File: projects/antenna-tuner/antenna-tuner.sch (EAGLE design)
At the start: 32 parts, among them J1 Power Jack, J2 RJ45, J3 RJ45, M1 SERVO, Q1 IRF5305, Q2 BC337, U1 Arduino Pro Mini

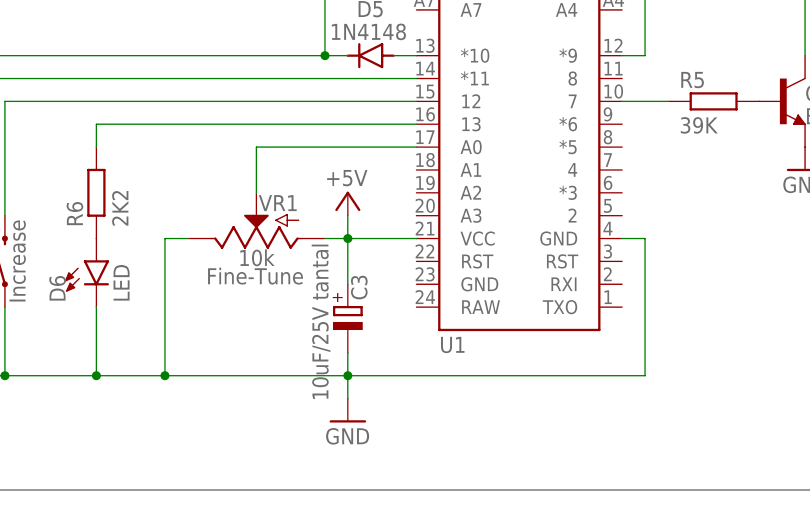
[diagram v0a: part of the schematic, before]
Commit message: Updated antenna tuner schematic
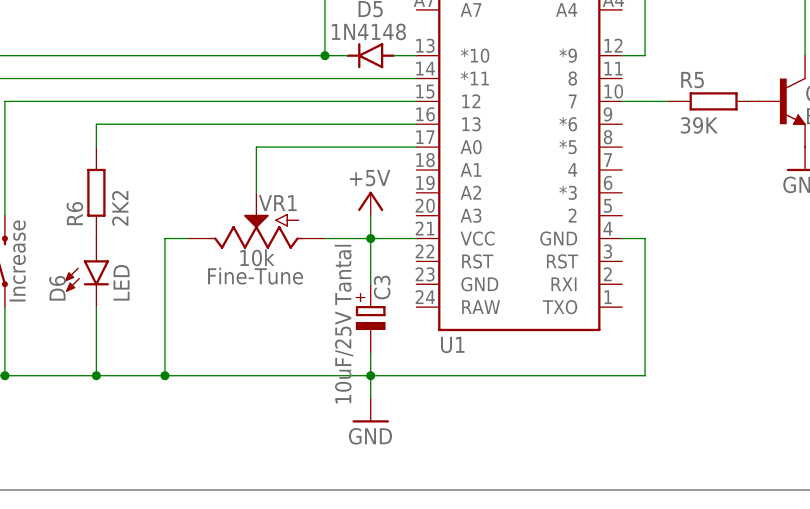
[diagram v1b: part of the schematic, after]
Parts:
- C3: value 10uF/25V tantal -> 10uF/25V Tantal
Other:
- moved on the sheet: C3
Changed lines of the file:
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@@
 <part name="J3" library="SparkFun-Connectors" library_urn="urn:adsk.eagle:library:513" deviceset="RJ45-8" device="" package3d_urn="urn:adsk.eagle:package:38235/1" value="RJ45"/>
 <part name="C1" library="rcl" library_urn="urn:adsk.eagle:library:334" deviceset="CPOL-EU" device="E5-10.5" package3d_urn="urn:adsk.eagle:package:23372/1" value="1000uF/25V"/>
-<part name="C3" library="rcl" library_urn="urn:adsk.eagle:library:334" deviceset="CPOL-EU" device="E2.5-6" package3d_urn="urn:adsk.eagle:package:23349/1" value="10uF/25V tantal"/>
+<part name="C3" library="rcl" library_urn="urn:adsk.eagle:library:334" deviceset="CPOL-EU" device="E2.5-6" package3d_urn="urn:adsk.eagle:package:23349/1" value="10uF/25V Tantal"/>
 <part name="R2" library="rcl" library_urn="urn:adsk.eagle:library:334" deviceset="R-EU_" device="0207/7" package3d_urn="urn:adsk.eagle:package:23493/2" value="196"/>
 <part name="R3" library="rcl" library_urn="urn:adsk.eagle:library:334" deviceset="R-EU_" device="0207/7" package3d_urn="urn:adsk.eagle:package:23493/2" value="196"/>
@@
 <attribute name="VALUE" x="-86.233" y="55.3466" size="1.778" layer="96"/>
 </instance>
-<instance part="C3" gate="G$1" x="10.16" y="17.78" smashed="yes">
-<attribute name="NAME" x="12.319" y="18.5166" size="1.778" layer="95" rot="R90"/>
-<attribute name="VALUE" x="8.001" y="7.3406" size="1.778" layer="96" rot="R90"/>
+<instance part="C3" gate="G$1" x="12.7" y="17.78" smashed="yes">
+<attribute name="NAME" x="14.859" y="18.5166" size="1.778" layer="95" rot="R90"/>
+<attribute name="VALUE" x="10.541" y="6.8326" size="1.778" layer="96" rot="R90"/>
 </instance>
 <instance part="R2" gate="G$1" x="-5.08" y="93.98" smashed="yes">
@@
 <attribute name="VALUE" x="0" y="24.13" size="1.778" layer="95" rot="R180" align="bottom-center"/>
 </instance>
-<instance part="P+4" gate="1" x="10.16" y="30.48" smashed="yes">
-<attribute name="VALUE" x="7.62" y="31.242" size="1.778" layer="96"/>
-</instance>
-<instance part="GND6" gate="1" x="10.16" y="5.08" smashed="yes">
-<attribute name="VALUE" x="7.62" y="2.54" size="1.778" layer="96"/>
+<instance part="P+4" gate="1" x="12.7" y="30.48" smashed="yes">
+<attribute name="VALUE" x="10.16" y="31.242" size="1.778" layer="96"/>
+</instance>
+<instance part="GND6" gate="1" x="12.7" y="5.08" smashed="yes">
+<attribute name="VALUE" x="10.16" y="2.54" size="1.778" layer="96"/>
 </instance>
 <instance part="R6" gate="G$1" x="-17.78" y="30.48" smashed="yes" rot="R90">
@@
 <pinref part="C3" gate="G$1" pin="-"/>
 <pinref part="GND6" gate="1" pin="GND"/>
-<wire x1="10.16" y1="7.62" x2="10.16" y2="10.16" width="0.1524" layer="91"/>
+<wire x1="12.7" y1="7.62" x2="12.7" y2="10.16" width="0.1524" layer="91"/>
 <pinref part="VR1" gate="G$1" pin="E"/>
-<wire x1="10.16" y1="10.16" x2="10.16" y2="12.7" width="0.1524" layer="91"/>
+<wire x1="12.7" y1="10.16" x2="12.7" y2="12.7" width="0.1524" layer="91"/>
 <wire x1="-7.62" y1="25.4" x2="-10.16" y2="25.4" width="0.1524" layer="91"/>
 <wire x1="-10.16" y1="25.4" x2="-10.16" y2="10.16" width="0.1524" layer="91"/>
-<wire x1="-10.16" y1="10.16" x2="10.16" y2="10.16" width="0.1524" layer="91"/>
-<junction x="10.16" y="10.16"/>
+<wire x1="-10.16" y1="10.16" x2="12.7" y2="10.16" width="0.1524" layer="91"/>
+<junction x="12.7" y="10.16"/>
 <pinref part="U1" gate="G$1" pin="GND"/>
 <wire x1="43.18" y1="10.16" x2="43.18" y2="25.4" width="0.1524" layer="91"/>
 <wire x1="43.18" y1="25.4" x2="40.64" y2="25.4" width="0.1524" layer="91"/>
-<wire x1="10.16" y1="10.16" x2="43.18" y2="10.16" width="0.1524" layer="91"/>
+<wire x1="12.7" y1="10.16" x2="43.18" y2="10.16" width="0.1524" layer="91"/>
 <pinref part="D6" gate="G$1" pin="C"/>
 <wire x1="-17.78" y1="17.78" x2="-17.78" y2="10.16" width="0.1524" layer="91"/>
@@
 <segment>
 <pinref part="C3" gate="G$1" pin="+"/>
-<wire x1="10.16" y1="20.32" x2="10.16" y2="25.4" width="0.1524" layer="91"/>
+<wire x1="12.7" y1="20.32" x2="12.7" y2="25.4" width="0.1524" layer="91"/>
 <pinref part="U1" gate="G$1" pin="VCC"/>
-<wire x1="10.16" y1="25.4" x2="17.78" y2="25.4" width="0.1524" layer="91"/>
+<wire x1="12.7" y1="25.4" x2="17.78" y2="25.4" width="0.1524" layer="91"/>
 <pinref part="P+4" gate="1" pin="+5V"/>
-<junction x="10.16" y="25.4"/>
-<wire x1="10.16" y1="25.4" x2="10.16" y2="27.94" width="0.1524" layer="91"/>
+<junction x="12.7" y="25.4"/>
+<wire x1="12.7" y1="25.4" x2="12.7" y2="27.94" width="0.1524" layer="91"/>
 <pinref part="VR1" gate="G$1" pin="A"/>
-<wire x1="7.62" y1="25.4" x2="10.16" y2="25.4" width="0.1524" layer="91"/>
-</segment>
-<segment>
+<wire x1="7.62" y1="25.4" x2="12.7" y2="25.4" width="0.1524" layer="91"/>
+</segment>
+<segment>
